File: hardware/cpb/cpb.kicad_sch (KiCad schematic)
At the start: 123 parts, among them J1 Conn_02x20_Odd_Even, J10 SW1, J11 SW2, J12 SW3, J13 PISW1, J14 μSW1, J15 μSW2, J16 μSW3, J17 μSW4, J2 I2CExt, J3 DAC1BUF, J4 DAC2BUF, J6 Conn_02x20_Odd_Even, J7 ADC6/7, J8 ADC2/3, J9 4FBRG, J99 RBFJUMP, Q1 PMBT2222A, Q2 IRF9393, Q3 MBT2222ADW1T1, Q4 PMBT2222A, U1 TS912, U2 ADR420ARMZ, U3 KF33BDT, U4 STM32L072R_B-Z_Tx, U5 AP62301WU, U6 SC16IS750xBS, Y1 14.7456MHz

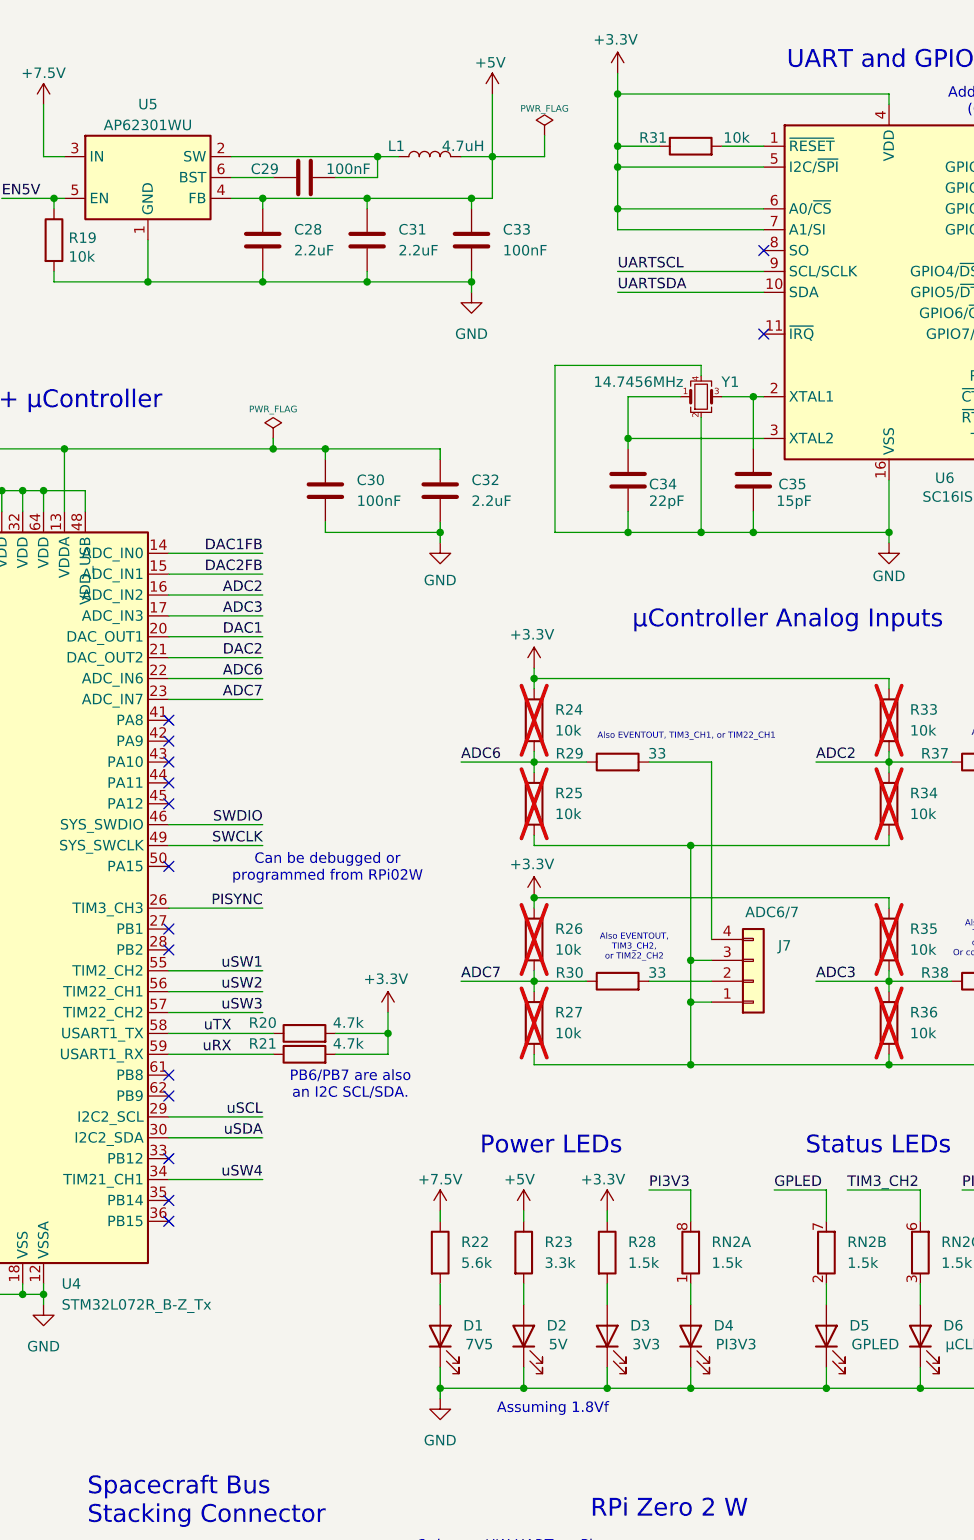
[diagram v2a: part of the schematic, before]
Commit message: cpb: continued work towards layout
- Adjust schematic; add datasheets, correct switcher output.  Additional
validation required.
- Adjust text.
- Add graphics
- Update design rules
- Perform an initial DRC in schematic & in layout.
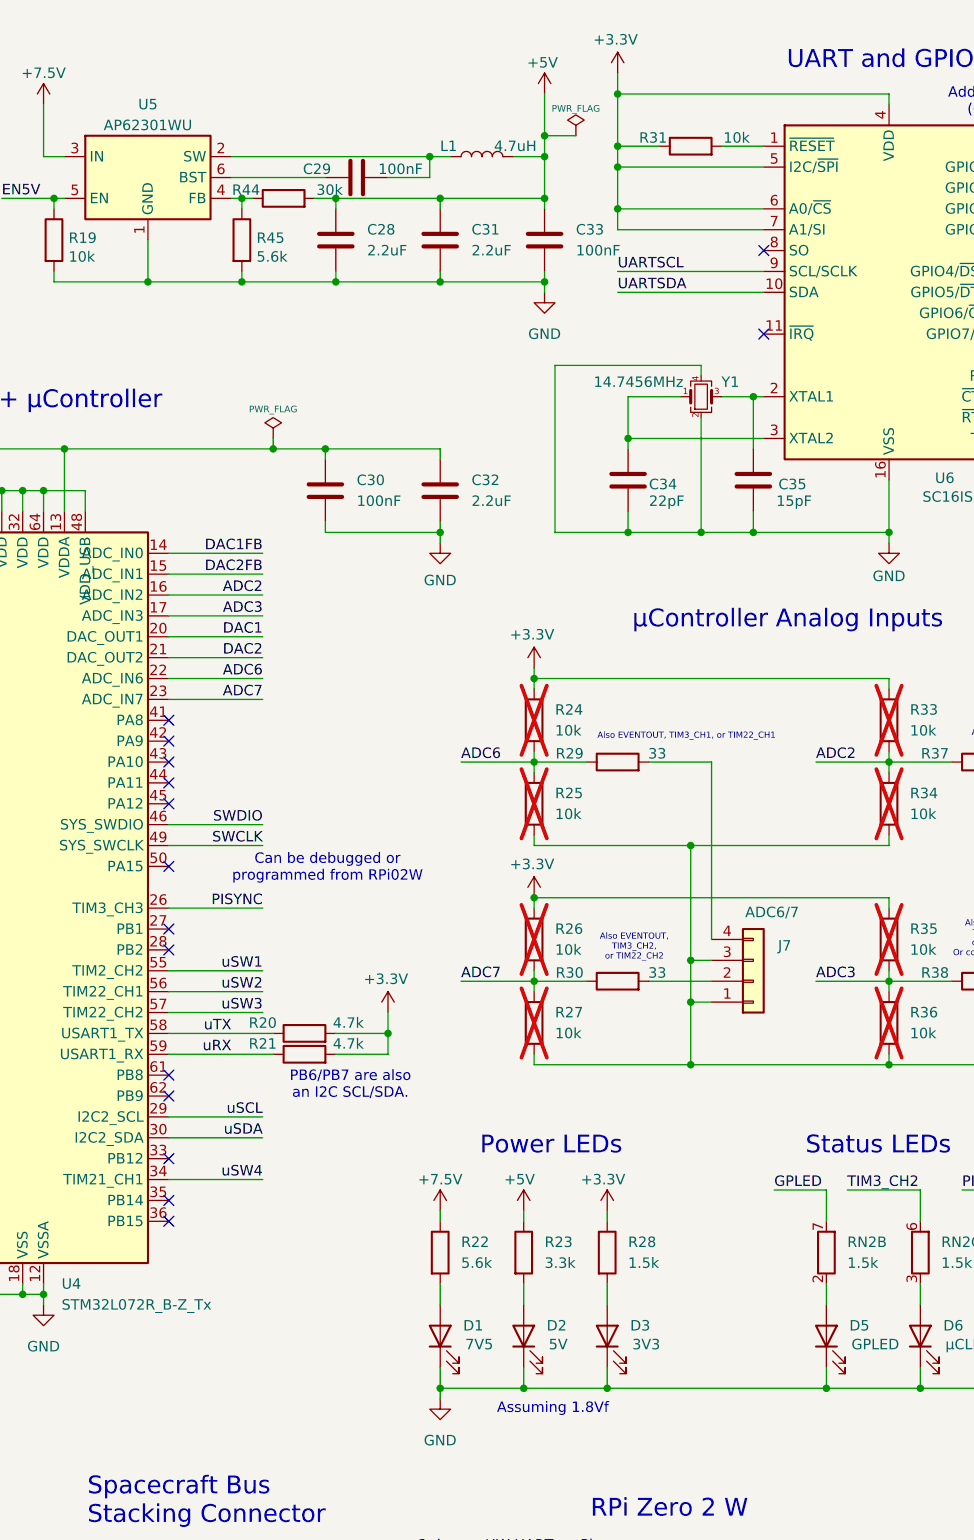
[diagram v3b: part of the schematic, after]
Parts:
- removed D4: PI3V3, LED_SMD:LED_0805_2012Metric, symbol Device:LED
- removed unit 1 of RN2
- added R44: 30k, Resistor_SMD:R_0603_1608Metric, symbol Device:R
- added R45: 5.6k, Resistor_SMD:R_0603_1608Metric, symbol Device:R
- J1: value Conn_02x20_Odd_Even -> Spacecraft Bus Stacking Connector
- J6: value Conn_02x20_Odd_Even -> Raspberry Pi Zero 2W
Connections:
- net +5V: now also R44.2; no longer U5.4 (FB)
- net GND: now also R45.2
- new net: R44.1, R45.1, U5.4 (FB)
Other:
- moved on the sheet: C28, C29, C31, C33, L1
